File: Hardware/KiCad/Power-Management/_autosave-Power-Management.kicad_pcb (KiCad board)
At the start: 2 copper layers, 108 x 67 mm, 57 parts, among them IC1 RT9080-33GJ5, J1 Screw_Terminal_01x02, J2 Conn_01x06, J3 Screw_Terminal_01x02, K1 FINDER-36.11, Q1 BC817, T1 ZMPT101B, U2 ACS758xCB-050B-PFF, U3 ESP-01, U4 LM358ADE4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

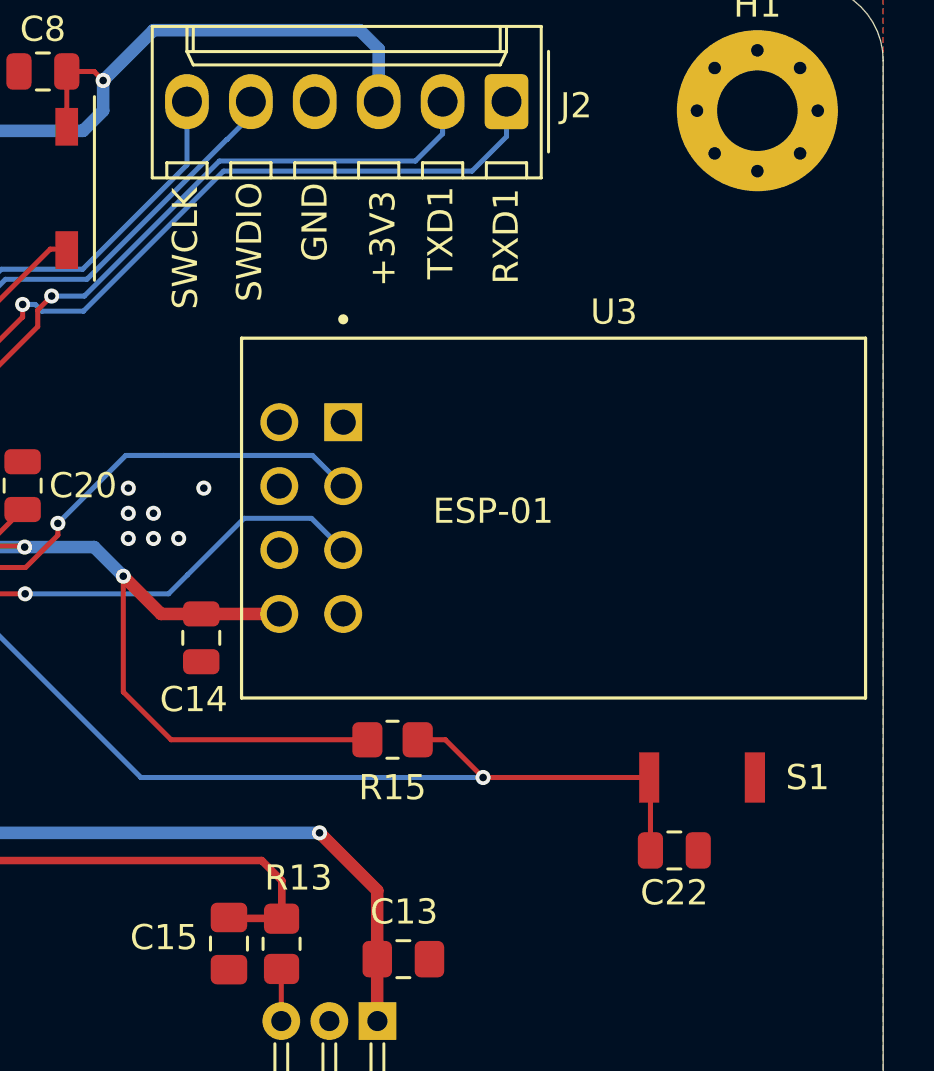
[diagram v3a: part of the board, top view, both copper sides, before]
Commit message: refactor: debug-uart silkscreen
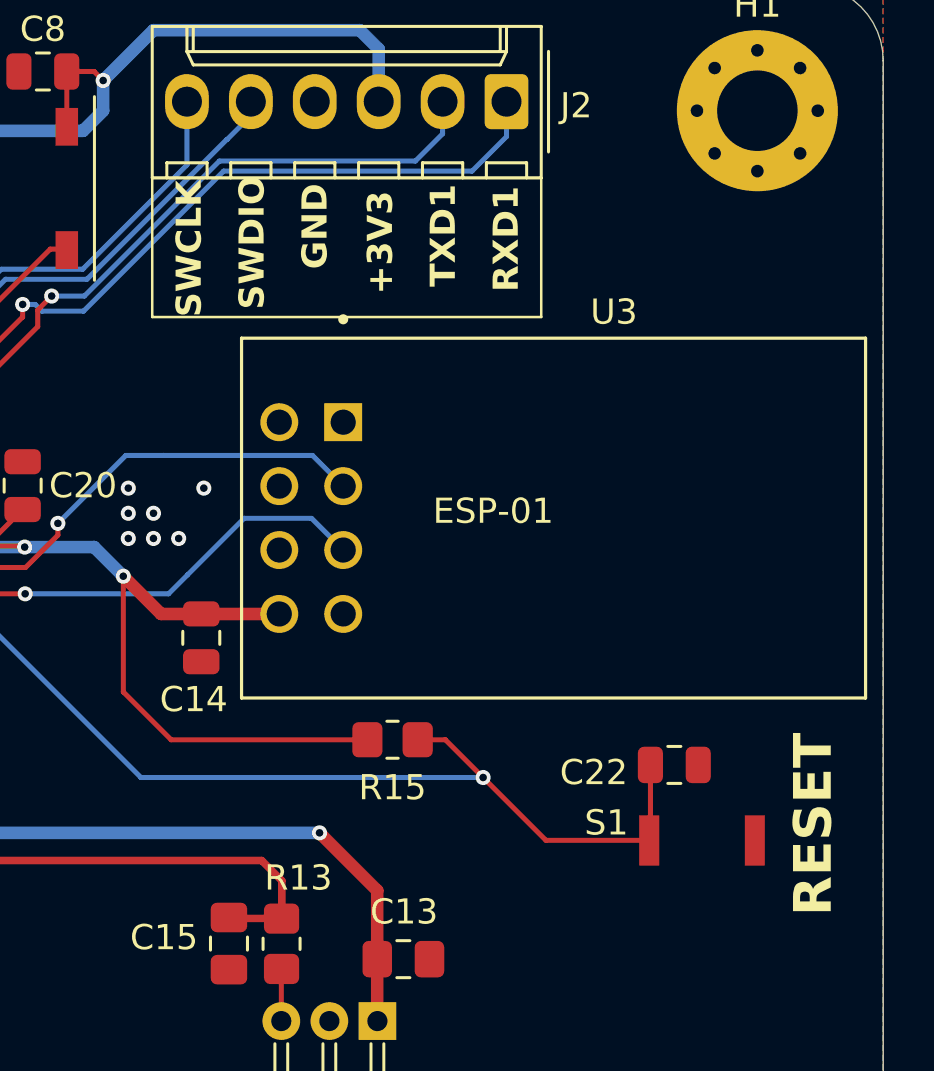
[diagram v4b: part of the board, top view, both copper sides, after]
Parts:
- moved C22 3.40 mm to (221.7, 81.0)
- moved S1 2.50 mm to (222.8, 84.0)
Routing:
- net Net-(U5-NRST): track 45.1 -> 45.9 mm
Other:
- board text added: "RESET"
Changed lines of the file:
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@@
 	(footprint "Capacitor_SMD:C_0805_2012Metric"
 		(layer "F.Cu")
-		(at 221.7 84.4 180)
+		(at 221.7 81 180)
 		(descr "Capacitor SMD 0805 (2012 Metric), square (rectangular) end terminal, IPC_7351 nominal, (Body size source: IPC-SM-782 page 76, https://www.pcb-3d.com/wordpress/wp-content/uploads/ipc-sm-782a_amendment_1_and_2.pdf, https://docs.google.com/spreadsheets/d/1BsfQQcO9C6DZCsRaXUlFlo91Tg2WpOkGARC1WS5S8t0/edit?usp=sharing), generated with kicad-footprint-generator")
 		(tags "capacitor")
 		(property "Reference" "C22"
-			(at 0 -1.68 360)
+			(at 3.2 -0.3 360)
 			(layer "F.SilkS")
 			(effects
@@
 	(footprint "SKRKAEE010:SKRK"
 		(layer "F.Cu")
-		(at 222.8 81.5 180)
+		(at 222.8 84 180)
 		(descr "<b>SKRK</b><br>")
 		(property "Reference" "S1"
-			(at -4.2 0 360)
+			(at 3.8 0.7 360)
 			(layer "F.SilkS")
 			(effects
@@
 		)
 	)
+	(gr_rect
+		(start 200.95 57.67)
+		(end 216.41 63.2)
+		(stroke
+			(width 0.1)
+			(type default)
+		)
+		(fill none)
+		(layer "F.SilkS")
+	)
 	(gr_arc
 		(start 149.5 75.5)
@@
 	)
 	(gr_text "TXD1\n"
-		(at 213 61.7 90)
-		(layer "F.SilkS")
+		(at 213.1 62 90)
+		(layer "F.SilkS" knockout)
 		(effects
 			(font
 				(size 1 1)
-				(thickness 0.1)
+				(thickness 0.25)
+				(bold yes)
 			)
 			(justify left bottom)
@@
 	)
 	(gr_text "SWDIO\n"
-		(at 205.4 62.6 90)
-		(layer "F.SilkS")
+		(at 205.5 62.9 90)
+		(layer "F.SilkS" knockout)
 		(effects
 			(font
 				(size 1 1)
-				(thickness 0.1)
+				(thickness 0.25)
+				(bold yes)
 			)
 			(justify left bottom)
@@
 	)
 	(gr_text "SWCLK\n"
-		(at 202.85 62.9 90)
-		(layer "F.SilkS")
+		(at 203 63.2 90)
+		(layer "F.SilkS" knockout)
 		(effects
 			(font
 				(size 1 1)
-				(thickness 0.1)
+				(thickness 0.25)
+				(bold yes)
 			)
 			(justify left bottom)
 		)
 	)
-	(gr_text "GND\n"
-		(at 208 61 90)
+	(gr_text "RESET"
+		(at 228.1 87 90)
 		(layer "F.SilkS")
 		(effects
 			(font
+				(size 1.5 1.5)
+				(thickness 0.3)
+				(bold yes)
+			)
+			(justify left bottom)
+		)
+	)
+	(gr_text "GND\n"
+		(at 208 61.3 90)
+		(layer "F.SilkS" knockout)
+		(effects
+			(font
 				(size 1 1)
-				(thickness 0.1)
+				(thickness 0.25)
+				(bold yes)
 			)
 			(justify left bottom)
@@
 	)
 	(gr_text "+3V3\n"
-		(at 210.7 62 90)
-		(layer "F.SilkS")
+		(at 210.6 62.3 90)
+		(layer "F.SilkS" knockout)
 		(effects
 			(font
 				(size 1 1)
-				(thickness 0.1)
+				(thickness 0.25)
+				(bold yes)
 			)
 			(justify left bottom)
@@
 	)
 	(gr_text "RXD1\n"
-		(at 215.6 61.9 90)
-		(layer "F.SilkS")
+		(at 215.6 62.2 90)
+		(layer "F.SilkS" knockout)
 		(effects
 			(font
 				(size 1 1)
-				(thickness 0.1)
+				(thickness 0.25)
+				(bold yes)
 			)
 			(justify left bottom)
@@
 	)
 	(segment
+		(start 220.75 83.95)
+		(end 220.7 84)
+		(width 0.2)
+		(layer "F.Cu")
+		(net 98)
+	)
+	(segment
 		(start 211.5 80)
 		(end 212.6 80)
@@
 	)
 	(segment
-		(start 212.6 80)
-		(end 214.1 81.5)
+		(start 216.6 84)
+		(end 220.7 84)
 		(width 0.2)
 		(layer "F.Cu")
@@
 	)
 	(segment
-		(start 220.75 84.4)
-		(end 220.75 81.55)
+		(start 212.6 80)
+		(end 214.1 81.5)
 		(width 0.2)
 		(layer "F.Cu")
@@
 	)
 	(segment
-		(start 217.4 81.5)
-		(end 220.7 81.5)
+		(start 187.325 72.65)
+		(end 187.325 72.655218)
 		(width 0.2)
 		(layer "F.Cu")
@@
 	)
 	(segment
-		(start 220.75 81.55)
-		(end 220.7 81.5)
+		(start 214.1 81.5)
+		(end 216.6 84)
 		(width 0.2)
 		(layer "F.Cu")
@@
 	)
 	(segment
-		(start 187.325 72.65)
-		(end 187.325 72.655218)
+		(start 220.75 81.4)
+		(end 220.75 83.95)
 		(width 0.2)
 		(layer "F.Cu")
@@
 	)
 	(segment
-		(start 214.1 81.5)
-		(end 217.4 81.5)
+		(start 220.7 81.35)
+		(end 220.75 81.4)
 		(width 0.2)
 		(layer "F.Cu")
@@
 		(min_thickness 0.125)
 		(filled_areas_thickness no)
-		(fill yes
+		(fill
 			(thermal_gap 0.5)
 			(thermal_bridge_width 0.5)
